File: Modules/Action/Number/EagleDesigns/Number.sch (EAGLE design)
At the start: 9 parts, among them U2 ATMEGA328P_TQFP

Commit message: fixed eagle files for new modules
SIN/SOUT was not correctly connected in them.
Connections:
- removed net 1X3SIN: U2.PC0(ADC0)
- net 1X3SIN-SOUT: now also U2.PC0(ADC0)
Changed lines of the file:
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@@
 <pinref part="R1" gate="G$1" pin="2"/>
+</segment>
+<segment>
+<pinref part="U2" gate="U$1" pin="PC0(ADC0)"/>
+<wire x1="208.28" y1="55.88" x2="228.6" y2="55.88" width="0.1524" layer="91"/>
+<junction x="228.6" y="55.88"/>
+<label x="210.82" y="55.88" size="1.778" layer="95"/>
 </segment>
 </net>
@@
 </segment>
 </net>
-<net name="1X3SIN" class="0">
-<segment>
-<pinref part="U2" gate="U$1" pin="PC0(ADC0)"/>
-<wire x1="208.28" y1="55.88" x2="220.98" y2="55.88" width="0.1524" layer="91"/>
-<junction x="220.98" y="55.88"/>
-<label x="210.82" y="55.88" size="1.778" layer="95"/>
-</segment>
-</net>

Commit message: Number: added final PCB #32
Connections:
- removed net SCL: U2.PC5(ADC5/SCL)
- removed net SDA: U2.PC4(ADC4/SDA)
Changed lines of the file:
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@@
-</segment>
-</net>
-<net name="SDA" class="0">
-<segment>
-<pinref part="U2" gate="U$1" pin="PC4(ADC4/SDA)"/>
-<wire x1="208.28" y1="45.72" x2="220.98" y2="45.72" width="0.1524" layer="91"/>
-<junction x="220.98" y="45.72"/>
-<label x="213.36" y="45.72" size="1.778" layer="95"/>
-</segment>
-</net>
-<net name="SCL" class="0">
-<segment>
-<pinref part="U2" gate="U$1" pin="PC5(ADC5/SCL)"/>
-<wire x1="208.28" y1="43.18" x2="220.98" y2="43.18" width="0.1524" layer="91"/>
-<junction x="220.98" y="43.18"/>
-<label x="213.36" y="43.18" size="1.778" layer="95"/>
 </segment>
 </net>

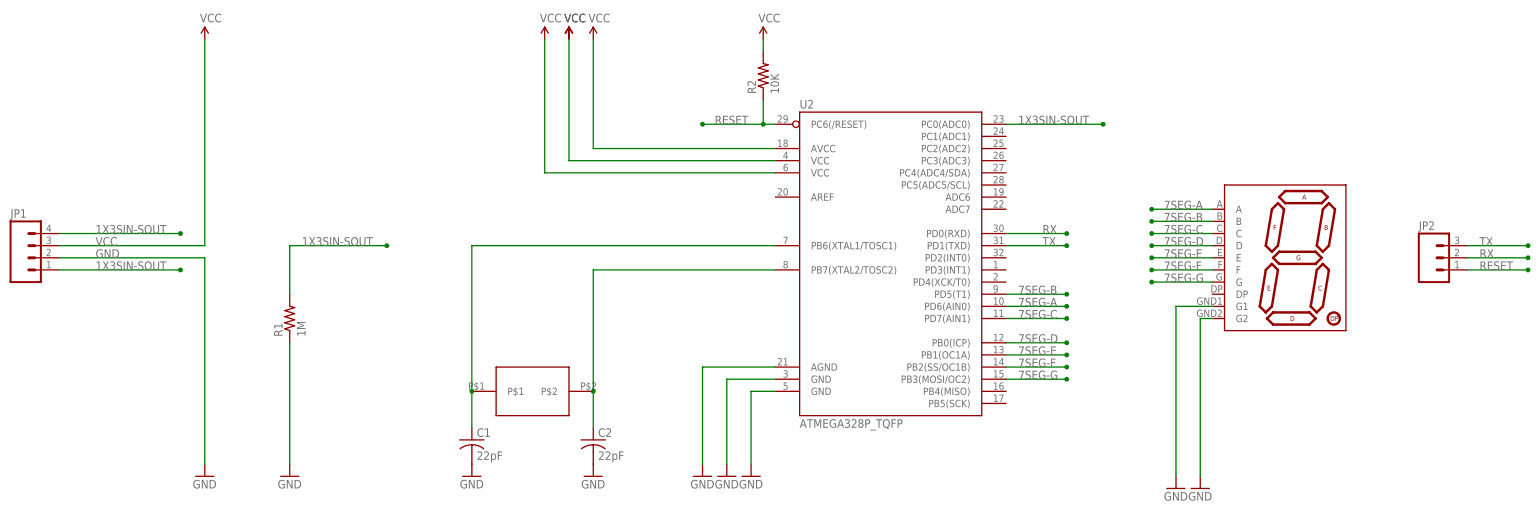
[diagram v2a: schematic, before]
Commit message: Removed crystal and added resistor on 7-seg
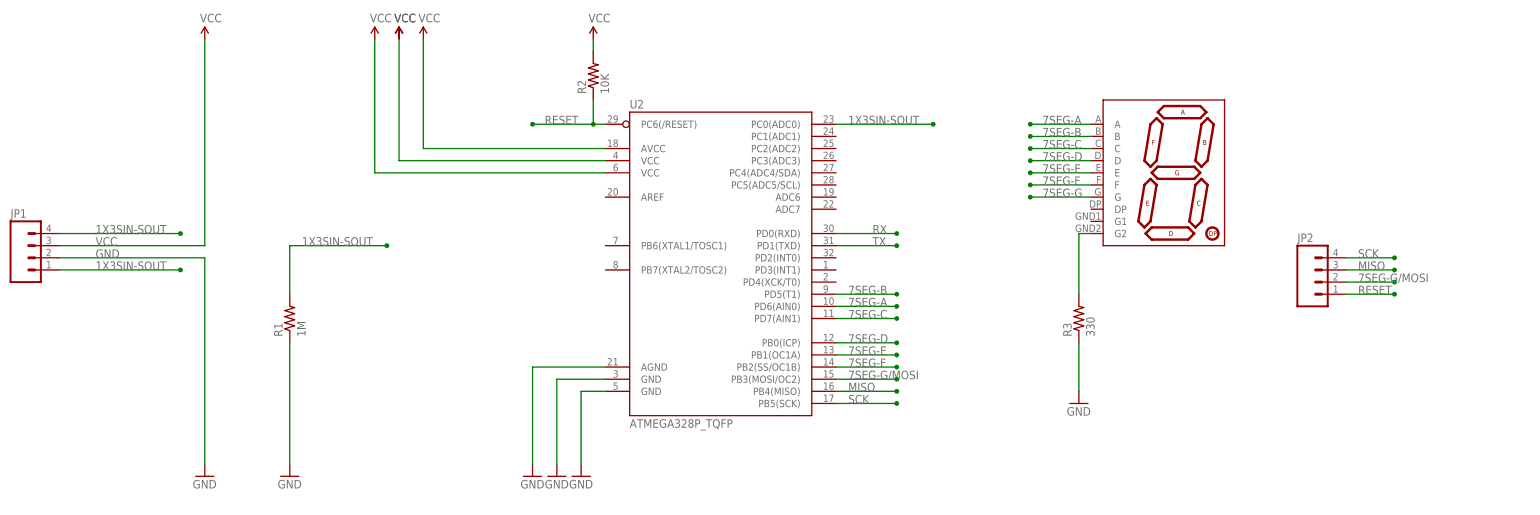
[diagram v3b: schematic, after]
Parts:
- removed C1, C2: 22pF, adafruit:C-USC0603
- removed U$2: NX503, MakerWear:NX503
- added R3: 330, resistor:R-US_R0603
- JP2: device SparkFun-Connectors:M03PTH -> SparkFun-Connectors:M04PTH
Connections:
- removed net N$3: C2.1, U$2.P$2, U2.PB7(XTAL2/TOSC2)
- new net 7SEG-G/MOSI: JP2.2, U2.PB3(MOSI/OC2)
- new net MISO: JP2.3, U2.PB4(MISO)
- new net SCK: JP2.4, U2.PB5(SCK)
- net 7SEG-G: no longer U2.PB3(MOSI/OC2)
- net GND: now also R3.1; no longer C1.2, C2.2, U$1.G1, U$1.G2
- net N$1: now also R3.2, U$1.G2; no longer C1.1, U$2.P$1, U2.PB6(XTAL1/TOSC1)
- net RX: no longer JP2.2
- net TX: no longer JP2.3
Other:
- moved on the sheet: R2, U2

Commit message: Number: removed crystal, modified for new bootloader #49
also added resistor to make sure that we address #49
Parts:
- removed R2: 10K, resistor:R-US_R0603
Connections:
- net 7SEG-G/MOSI renamed MOSI
- removed net RX: U2.PD0(RXD)
- removed net TX: U2.PD1(TXD)
- net 7SEG-A: now also U2.PB2(SS/OC1B); no longer U2.PD6(AIN0)
- net 7SEG-B: now also U2.PB1(OC1A); no longer U2.PD5(T1)
- net 7SEG-C: now also U2.PD0(RXD); no longer U2.PD7(AIN1)
- net 7SEG-D: now also U2.PD1(TXD); no longer U2.PB0(ICP)
- net 7SEG-E: now also U2.PD2(INT0); no longer U2.PB1(OC1A)
- net 7SEG-F: now also U2.PB0(ICP); no longer U2.PB2(SS/OC1B)
- net 7SEG-G: now also U2.PD5(T1)
- net RESET: no longer R2.1
- net VCC: no longer R2.2
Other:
- moved on the sheet: JP2
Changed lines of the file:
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@@
 <?xml version="1.0" encoding="utf-8"?>
 <!DOCTYPE eagle SYSTEM "eagle.dtd">
-<eagle version="7.6.0">
+<eagle version="7.3.0">
 <drawing>
 <settings>
@@
 <part name="SUPPLY2" library="SparkFun-Aesthetics" deviceset="VCC" device=""/>
 <part name="SUPPLY5" library="SparkFun-Aesthetics" deviceset="VCC" device=""/>
-<part name="R2" library="resistor" deviceset="R-US_" device="R0603" value="10K"/>
-<part name="SUPPLY6" library="SparkFun-Aesthetics" deviceset="VCC" device=""/>
 <part name="SUPPLY7" library="SparkFun-Aesthetics" deviceset="VCC" device=""/>
 <part name="SUPPLY8" library="SparkFun-Aesthetics" deviceset="VCC" device=""/>
@@
 <instance part="SUPPLY2" gate="G$1" x="81.28" y="73.66"/>
 <instance part="SUPPLY5" gate="G$1" x="76.2" y="73.66"/>
-<instance part="R2" gate="G$1" x="121.92" y="66.04" rot="R90"/>
-<instance part="SUPPLY6" gate="G$1" x="121.92" y="73.66"/>
 <instance part="SUPPLY7" gate="G$1" x="81.28" y="73.66"/>
 <instance part="SUPPLY8" gate="G$1" x="86.36" y="73.66"/>
@@
 <instance part="U$1" gate="G$1" x="241.3" y="45.72"/>
 <instance part="GND3" gate="1" x="223.52" y="-2.54"/>
-<instance part="JP2" gate="G$1" x="274.32" y="22.86"/>
+<instance part="JP2" gate="G$1" x="276.86" y="27.94"/>
 <instance part="R3" gate="G$1" x="223.52" y="15.24" rot="R90"/>
 </instances>
@@
 </segment>
 <segment>
-<pinref part="R2" gate="G$1" pin="2"/>
-<wire x1="121.92" y1="71.12" x2="121.92" y2="73.66" width="0.1524" layer="91"/>
-<pinref part="SUPPLY6" gate="G$1" pin="VCC"/>
-</segment>
-<segment>
 <pinref part="U2" gate="U$1" pin="AVCC"/>
 <wire x1="124.46" y1="50.8" x2="86.36" y2="50.8" width="0.1524" layer="91"/>
@@
 <segment>
 <pinref part="U2" gate="U$1" pin="PC6(/RESET)"/>
-<wire x1="124.46" y1="55.88" x2="121.92" y2="55.88" width="0.1524" layer="91"/>
-<wire x1="121.92" y1="55.88" x2="121.92" y2="60.96" width="0.1524" layer="91"/>
-<pinref part="R2" gate="G$1" pin="1"/>
-<wire x1="121.92" y1="55.88" x2="109.22" y2="55.88" width="0.1524" layer="91"/>
-<junction x="121.92" y="55.88"/>
+<wire x1="124.46" y1="55.88" x2="109.22" y2="55.88" width="0.1524" layer="91"/>
 <label x="111.76" y="55.88" size="1.778" layer="95"/>
 <junction x="109.22" y="55.88"/>
@@
 <segment>
 <pinref part="JP2" gate="G$1" pin="1"/>
-<wire x1="279.4" y1="20.32" x2="289.56" y2="20.32" width="0.1524" layer="91"/>
-<label x="281.94" y="20.32" size="1.778" layer="95"/>
-<junction x="289.56" y="20.32"/>
-</segment>
-</net>
-<net name="RX" class="0">
-<segment>
-<pinref part="U2" gate="U$1" pin="PD0(RXD)"/>
-<wire x1="172.72" y1="33.02" x2="185.42" y2="33.02" width="0.1524" layer="91"/>
-<junction x="185.42" y="33.02"/>
-<label x="180.34" y="33.02" size="1.778" layer="95"/>
-</segment>
-</net>
-<net name="TX" class="0">
-<segment>
-<pinref part="U2" gate="U$1" pin="PD1(TXD)"/>
-<wire x1="172.72" y1="30.48" x2="185.42" y2="30.48" width="0.1524" layer="91"/>
-<junction x="185.42" y="30.48"/>
-<label x="180.34" y="30.48" size="1.778" layer="95"/>
+<wire x1="281.94" y1="25.4" x2="294.64" y2="25.4" width="0.1524" layer="91"/>
+<label x="284.48" y="25.4" size="1.778" layer="95"/>
+<junction x="294.64" y="25.4"/>
 </segment>
 </net>
@@
 </segment>
 <segment>
-<pinref part="U2" gate="U$1" pin="PD6(AIN0)"/>
-<wire x1="172.72" y1="17.78" x2="185.42" y2="17.78" width="0.1524" layer="91"/>
-<junction x="185.42" y="17.78"/>
-<label x="175.26" y="17.78" size="1.778" layer="95"/>
+<pinref part="U2" gate="U$1" pin="PB2(SS/OC1B)"/>
+<wire x1="172.72" y1="5.08" x2="185.42" y2="5.08" width="0.1524" layer="91"/>
+<label x="175.26" y="5.08" size="1.778" layer="95"/>
+<junction x="185.42" y="5.08"/>
 </segment>
 </net>
@@
 </segment>
 <segment>
-<pinref part="U2" gate="U$1" pin="PD5(T1)"/>
-<wire x1="172.72" y1="20.32" x2="185.42" y2="20.32" width="0.1524" layer="91"/>
-<junction x="185.42" y="20.32"/>
-<label x="175.26" y="20.32" size="1.778" layer="95"/>
+<pinref part="U2" gate="U$1" pin="PB1(OC1A)"/>
+<wire x1="172.72" y1="7.62" x2="185.42" y2="7.62" width="0.1524" layer="91"/>
+<label x="175.26" y="7.62" size="1.778" layer="95"/>
+<junction x="185.42" y="7.62"/>
 </segment>
 </net>
 <net name="7SEG-C" class="0">
-<segment>
-<pinref part="U2" gate="U$1" pin="PD7(AIN1)"/>
-<wire x1="172.72" y1="15.24" x2="185.42" y2="15.24" width="0.1524" layer="91"/>
-<junction x="185.42" y="15.24"/>
-<label x="175.26" y="15.24" size="1.778" layer="95"/>
-</segment>
 <segment>
 <pinref part="U$1" gate="G$1" pin="C"/>
@@
 <label x="215.9" y="50.8" size="1.778" layer="95"/>
 </segment>
+<segment>
+<pinref part="U2" gate="U$1" pin="PD0(RXD)"/>
+<wire x1="172.72" y1="33.02" x2="185.42" y2="33.02" width="0.1524" layer="91"/>
+<label x="175.26" y="33.02" size="1.778" layer="95"/>
+<junction x="185.42" y="33.02"/>
+</segment>
 </net>
 <net name="7SEG-D" class="0">
-<segment>
-<pinref part="U2" gate="U$1" pin="PB0(ICP)"/>
-<wire x1="172.72" y1="10.16" x2="185.42" y2="10.16" width="0.1524" layer="91"/>
-<junction x="185.42" y="10.16"/>
-<label x="175.26" y="10.16" size="1.778" layer="95"/>
-</segment>
 <segment>
 <pinref part="U$1" gate="G$1" pin="D"/>
@@
 <label x="215.9" y="48.26" size="1.778" layer="95"/>
 </segment>
+<segment>
+<pinref part="U2" gate="U$1" pin="PD1(TXD)"/>
+<wire x1="172.72" y1="30.48" x2="185.42" y2="30.48" width="0.1524" layer="91"/>
+<label x="175.26" y="30.48" size="1.778" layer="95"/>
+<junction x="185.42" y="30.48"/>
+</segment>
 </net>
 <net name="7SEG-E" class="0">
-<segment>
-<pinref part="U2" gate="U$1" pin="PB1(OC1A)"/>
-<wire x1="172.72" y1="7.62" x2="185.42" y2="7.62" width="0.1524" layer="91"/>
-<junction x="185.42" y="7.62"/>
-<label x="175.26" y="7.62" size="1.778" layer="95"/>
-</segment>
 <segment>
 <pinref part="U$1" gate="G$1" pin="E"/>
@@
 <label x="215.9" y="45.72" size="1.778" layer="95"/>
 </segment>
+<segment>
+<pinref part="U2" gate="U$1" pin="PD2(INT0)"/>
+<wire x1="172.72" y1="27.94" x2="185.42" y2="27.94" width="0.1524" layer="91"/>
+<label x="175.26" y="27.94" size="1.778" layer="95"/>
+<junction x="185.42" y="27.94"/>
+</segment>
 </net>
 <net name="7SEG-F" class="0">
-<segment>
-<pinref part="U2" gate="U$1" pin="PB2(SS/OC1B)"/>
-<wire x1="172.72" y1="5.08" x2="185.42" y2="5.08" width="0.1524" layer="91"/>
-<junction x="185.42" y="5.08"/>
-<label x="175.26" y="5.08" size="1.778" layer="95"/>
-</segment>
 <segment>
 <pinref part="U$1" gate="G$1" pin="F"/>
@@
 <label x="215.9" y="43.18" size="1.778" layer="95"/>
 </segment>
+<segment>
+<pinref part="U2" gate="U$1" pin="PB0(ICP)"/>
+<wire x1="172.72" y1="10.16" x2="185.42" y2="10.16" width="0.1524" layer="91"/>
+<label x="175.26" y="10.16" size="1.778" layer="95"/>
+<junction x="185.42" y="10.16"/>
+</segment>
 </net>
 <net name="7SEG-G" class="0">
@@
 <label x="215.9" y="40.64" size="1.778" layer="95"/>
 </segment>
+<segment>
+<pinref part="U2" gate="U$1" pin="PD5(T1)"/>
+<wire x1="172.72" y1="20.32" x2="185.42" y2="20.32" width="0.1524" layer="91"/>
+<label x="175.26" y="20.32" size="1.778" layer="95"/>
+<junction x="185.42" y="20.32"/>
+</segment>
 </net>
 <net name="N$1" class="0">
@@
 <segment>
 <pinref part="JP2" gate="G$1" pin="4"/>
-<wire x1="279.4" y1="27.94" x2="289.56" y2="27.94" width="0.1524" layer="91"/>
-<label x="281.94" y="27.94" size="1.778" layer="95"/>
-<junction x="289.56" y="27.94"/>
+<wire x1="281.94" y1="33.02" x2="294.64" y2="33.02" width="0.1524" layer="91"/>
+<label x="284.48" y="33.02" size="1.778" layer="95"/>
+<junction x="294.64" y="33.02"/>
 </segment>
 <segment>
@@
 <segment>
 <pinref part="JP2" gate="G$1" pin="3"/>
-<wire x1="279.4" y1="25.4" x2="289.56" y2="25.4" width="0.1524" layer="91"/>
-<label x="281.94" y="25.4" size="1.778" layer="95"/>
-<junction x="289.56" y="25.4"/>
+<wire x1="281.94" y1="30.48" x2="294.64" y2="30.48" width="0.1524" layer="91"/>
+<label x="284.48" y="30.48" size="1.778" layer="95"/>
+<junction x="294.64" y="30.48"/>
 </segment>
 <segment>
@@
 </segment>
 </net>
-<net name="7SEG-G/MOSI" class="0">
+<net name="MOSI" class="0">
 <segment>
 <pinref part="U2" gate="U$1" pin="PB3(MOSI/OC2)"/>
 <wire x1="172.72" y1="2.54" x2="185.42" y2="2.54" width="0.1524" layer="91"/>
+<label x="175.26" y="2.54" size="1.778" layer="95"/>
 <junction x="185.42" y="2.54"/>
-<label x="175.26" y="2.54" size="1.778" layer="95"/>
 </segment>
 <segment>
 <pinref part="JP2" gate="G$1" pin="2"/>
-<wire x1="279.4" y1="22.86" x2="289.56" y2="22.86" width="0.1524" layer="91"/>
-<label x="281.94" y="22.86" size="1.778" layer="95"/>
-<junction x="289.56" y="22.86"/>
-</segment>
-</net>
+<wire x1="281.94" y1="27.94" x2="294.64" y2="27.94" width="0.1524" layer="91"/>
+<label x="284.48" y="27.94" size="1.778" layer="95"/>
+<junction x="294.64" y="27.94"/>
+</segment>
+</net>
